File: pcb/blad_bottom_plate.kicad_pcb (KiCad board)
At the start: 2 copper layers, 228.6 x 76.2 mm, 8 parts

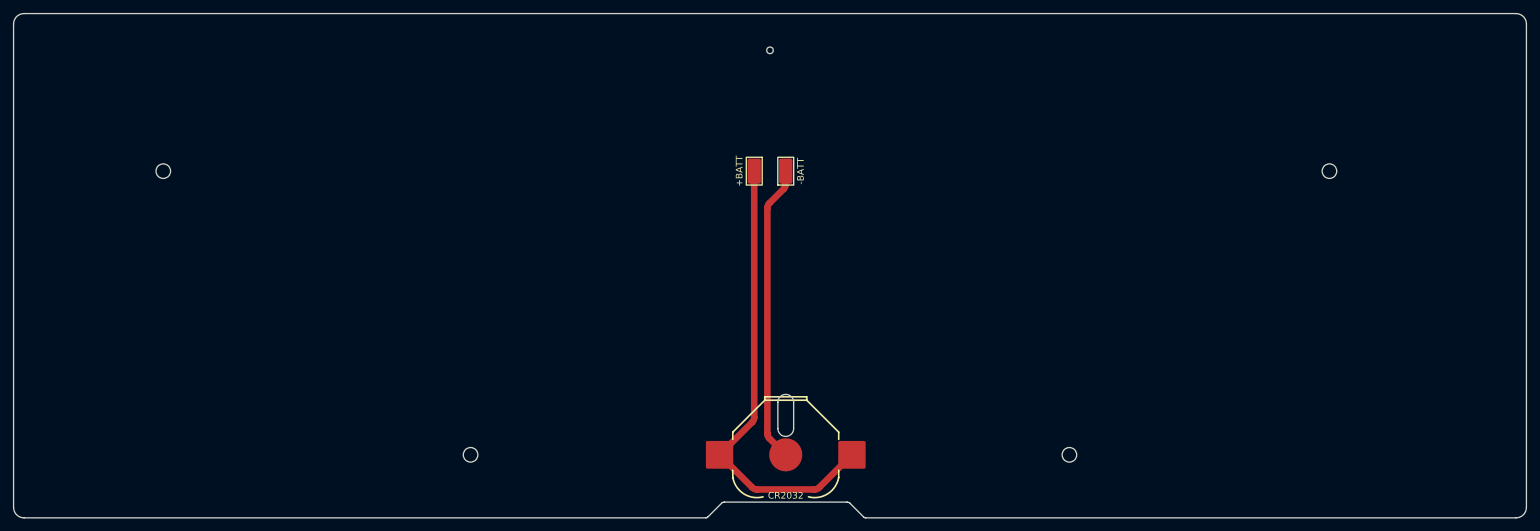
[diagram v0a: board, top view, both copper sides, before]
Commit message: Update PCB and plate designs
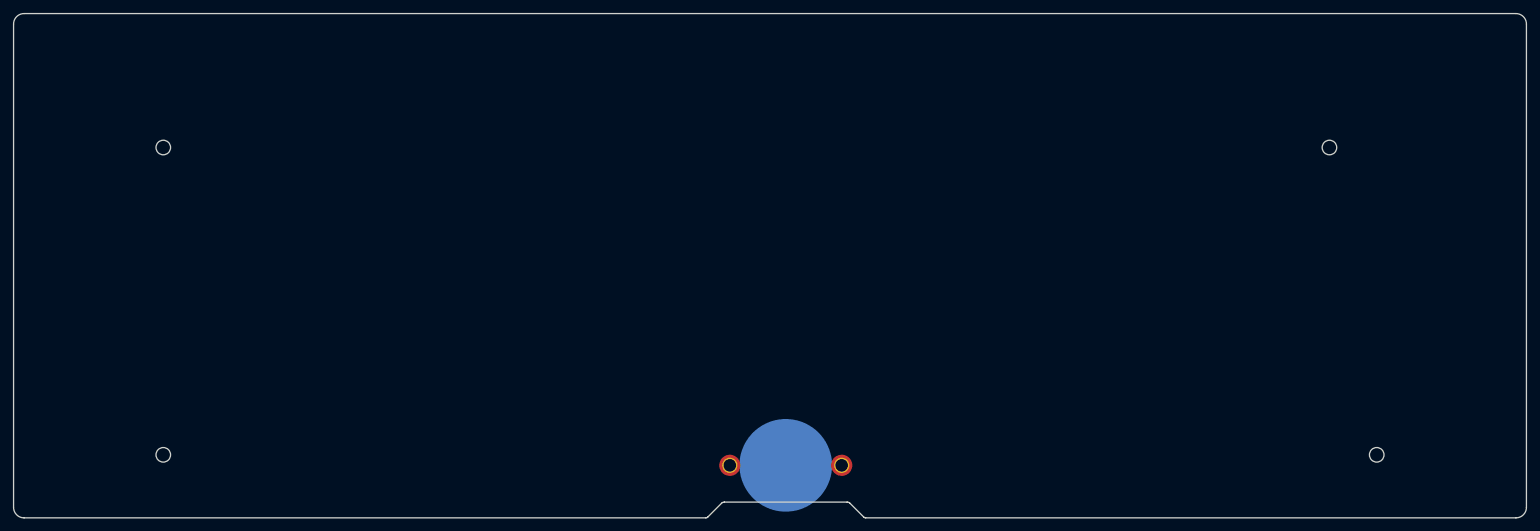
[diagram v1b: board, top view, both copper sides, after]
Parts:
- removed TP1: +BATT, TestPoint:TestPoint_Keystone_5019_Miniature
- removed TP2: -BATT, TestPoint:TestPoint_Keystone_5019_Miniature
- added G***: LOGO, Smidr:logo, B.Cu at (233.6, 175.6)
- BT1: value CR2032 -> Battery_Cell; footprint Smidr:BAT-SMD_MY-1632-03 -> Smidr:BatteryHolder_Takachi_BS-S-1632; moved to B.Cu
- moved G*** 64.8 mm to (192.5, 172.6)
- moved REF** 46.4 mm to (112.3, 176.2)
- moved REF** 46.4 mm to (295.7, 176.2)
- moved REF** 3.57 mm to (112.3, 129.8)
- moved REF** 3.57 mm to (288.5, 129.8)
- moved BT1 1.59 mm to (206.4, 177.8), turned to 180 degrees
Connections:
- BT1 pad 1: +BATT -> (no net)
- BT1 pad 2: GND -> (no net)
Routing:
- net +BATT: track 69.2 -> 0.00 mm
- net GND: track 45.0 -> 0.00 mm
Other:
- outline, holes or cut-outs redrawn
- board text removed: "Blað"

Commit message: Update bottom plate thickness and layout
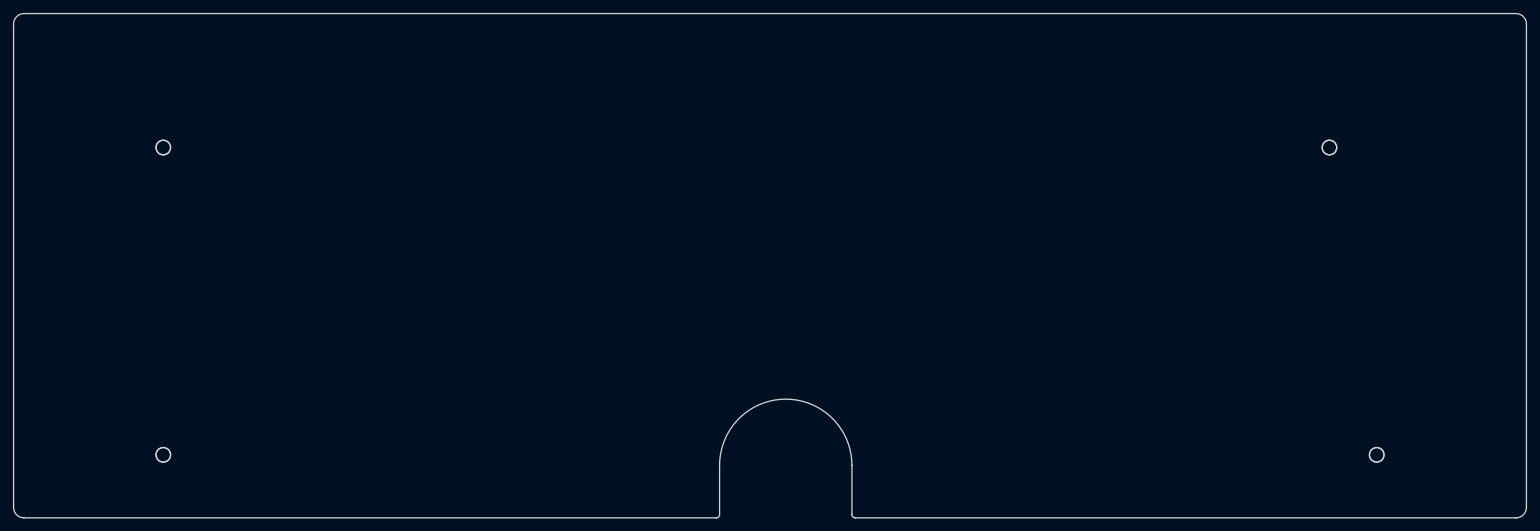
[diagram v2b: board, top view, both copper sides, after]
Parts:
- removed BT1: Battery_Cell, Smidr:BatteryHolder_Takachi_BS-S-1632
- moved G*** 3.18 mm to (192.5, 175.8)
- moved G*** 3.17 mm to (233.6, 178.8)
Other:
- outline, holes or cut-outs redrawn
